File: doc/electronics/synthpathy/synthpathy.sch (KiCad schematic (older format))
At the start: 56 parts, among them J1 midi_in_port, J2 midi_out_port, SW1 btn0, SW10 btn9, SW11 btn10, SW12 btn11, SW13 btn12, SW14 btn13, SW15 btn14, SW16 btn15, SW17 btn16, SW18 btn17, SW19 btn18, SW2 btn1, SW20 btn19, SW21 btn20, SW22 btn21, SW23 btn22, SW24 btn23, SW25 btn24, SW3 btn2, SW4 btn3, SW5 btn4, SW6 btn5, SW7 btn6, SW8 btn7, SW9 btn8, U1 Raspberry Pico, U2 4N35

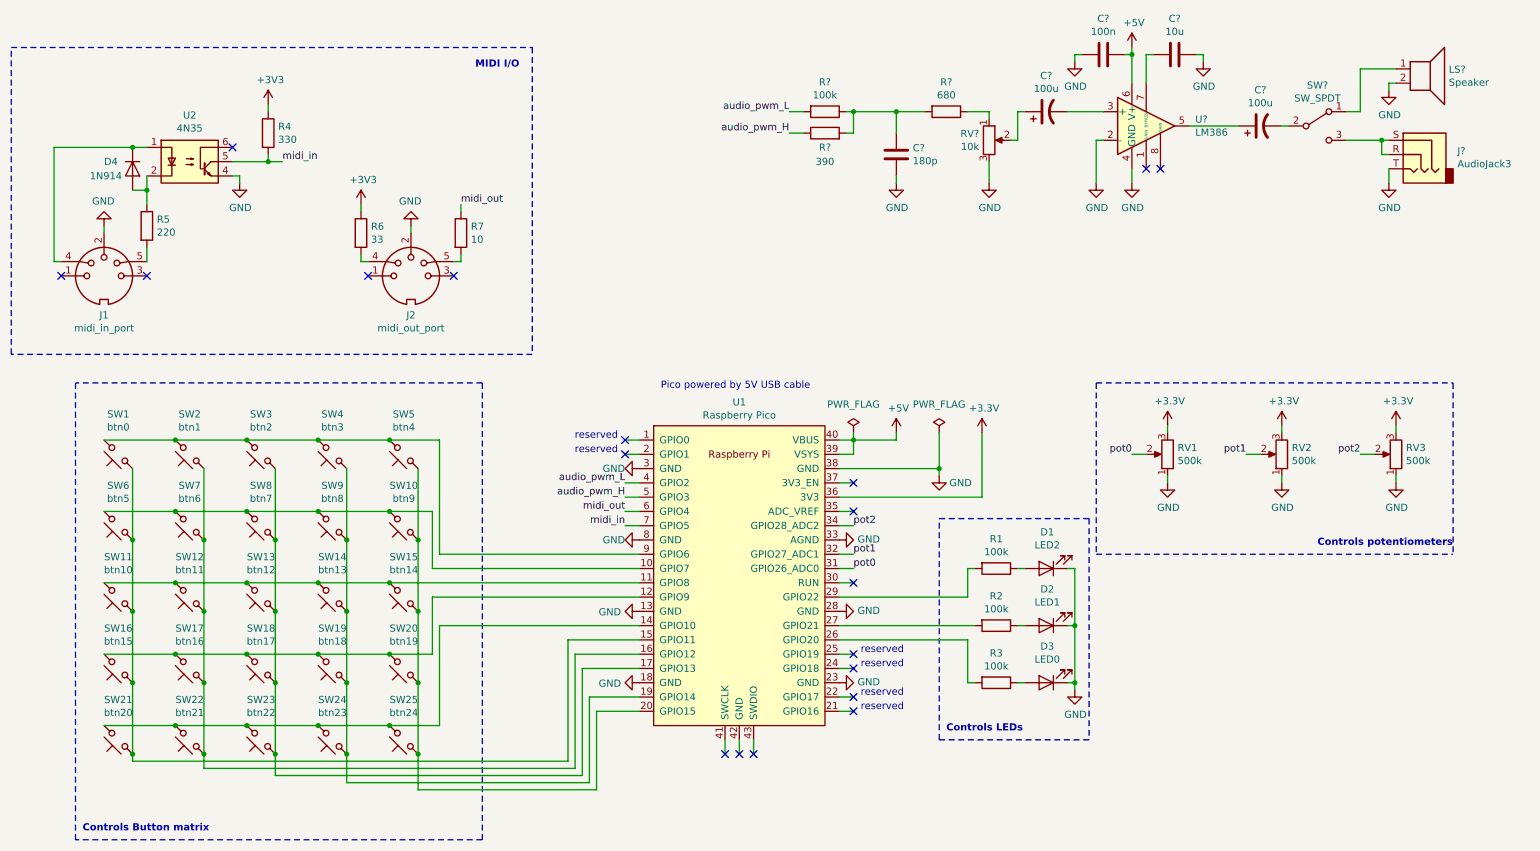
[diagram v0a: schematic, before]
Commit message: Updated schematics and comments
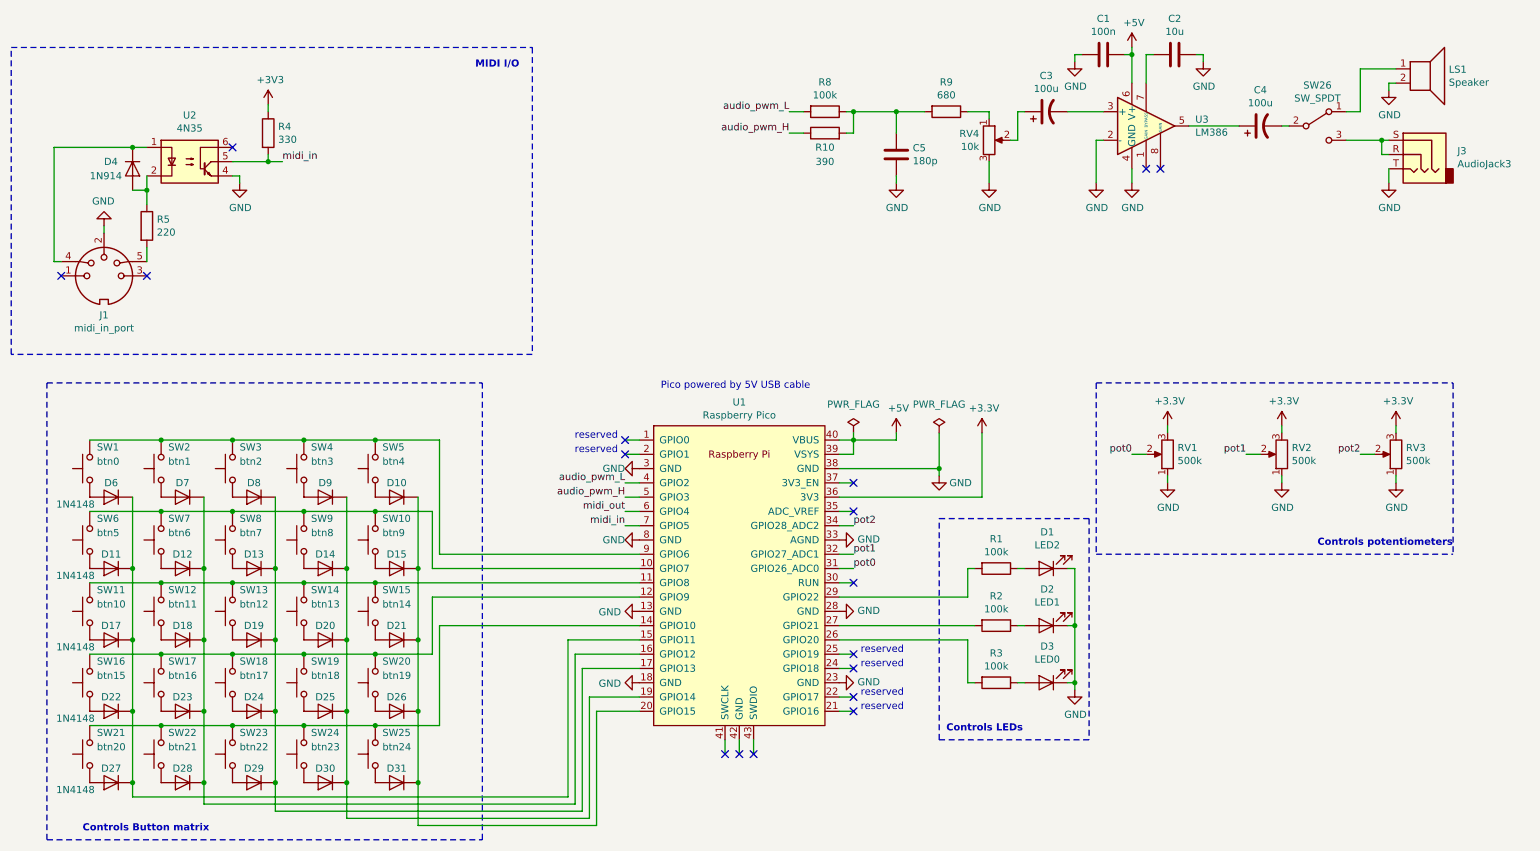
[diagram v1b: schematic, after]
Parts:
- removed J2: midi_out_port, symbol Connector:DIN-5_180degree
- removed R6: 33, symbol Device:R
- removed R7: 10, symbol Device:R
- removed SW1: btn0, symbol Switch:SW_Push_45deg
- removed SW10: btn9, symbol Switch:SW_Push_45deg
- removed SW11: btn10, symbol Switch:SW_Push_45deg
- removed SW12: btn11, symbol Switch:SW_Push_45deg
- removed SW13: btn12, symbol Switch:SW_Push_45deg
- removed SW14: btn13, symbol Switch:SW_Push_45deg
- removed SW15: btn14, symbol Switch:SW_Push_45deg
- removed SW16: btn15, symbol Switch:SW_Push_45deg
- removed SW17: btn16, symbol Switch:SW_Push_45deg
- removed SW18: btn17, symbol Switch:SW_Push_45deg
- removed SW19: btn18, symbol Switch:SW_Push_45deg
- removed SW2: btn1, symbol Switch:SW_Push_45deg
- removed SW20: btn19, symbol Switch:SW_Push_45deg
- removed SW21: btn20, symbol Switch:SW_Push_45deg
- removed SW22: btn21, symbol Switch:SW_Push_45deg
- removed SW23: btn22, symbol Switch:SW_Push_45deg
- removed SW24: btn23, symbol Switch:SW_Push_45deg
- removed SW25: btn24, symbol Switch:SW_Push_45deg
- removed SW3: btn2, symbol Switch:SW_Push_45deg
- removed SW4: btn3, symbol Switch:SW_Push_45deg
- removed SW5: btn4, symbol Switch:SW_Push_45deg
- removed SW6: btn5, symbol Switch:SW_Push_45deg
- removed SW7: btn6, symbol Switch:SW_Push_45deg
- removed SW8: btn7, symbol Switch:SW_Push_45deg
- removed SW9: btn8, symbol Switch:SW_Push_45deg
- added D10, D11, D12, D13, D14, D15, D17, D18, D19, D20, D21, D22, D23, D24, D25, D26, D27, D28, D29, D30, D31, D6, D7, D8, D9: 1N4148, Diode_THT:D_DO-35_SOD27_P7.62mm_Horizontal, symbol Diode:1N4148
- added SW1: btn0, symbol Switch:SW_Push
- added SW10: btn9, symbol Switch:SW_Push
- added SW11: btn10, symbol Switch:SW_Push
- added SW12: btn11, symbol Switch:SW_Push
- added SW13: btn12, symbol Switch:SW_Push
- added SW14: btn13, symbol Switch:SW_Push
- added SW15: btn14, symbol Switch:SW_Push
- added SW16: btn15, symbol Switch:SW_Push
- added SW17: btn16, symbol Switch:SW_Push
- added SW18: btn17, symbol Switch:SW_Push
- added SW19: btn18, symbol Switch:SW_Push
- added SW2: btn1, symbol Switch:SW_Push
- added SW20: btn19, symbol Switch:SW_Push
- added SW21: btn20, symbol Switch:SW_Push
- added SW22: btn21, symbol Switch:SW_Push
- added SW23: btn22, symbol Switch:SW_Push
- added SW24: btn23, symbol Switch:SW_Push
- added SW25: btn24, symbol Switch:SW_Push
- added SW3: btn2, symbol Switch:SW_Push
- added SW4: btn3, symbol Switch:SW_Push
- added SW5: btn4, symbol Switch:SW_Push
- added SW6: btn5, symbol Switch:SW_Push
- added SW7: btn6, symbol Switch:SW_Push
- added SW8: btn7, symbol Switch:SW_Push
- added SW9: btn8, symbol Switch:SW_Push
- gave numbers to parts that had none: 13
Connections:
- net at U1.10 (GPIO7): now also SW10.2, SW6.2, SW7.2, SW8.2, SW9.2
- net at U1.11 (GPIO8): now also SW11.2, SW12.2, SW13.2, SW14.2, SW15.2
- net at U1.12 (GPIO9): now also SW16.2, SW17.2, SW18.2, SW19.2, SW20.2
- net at U1.14 (GPIO10): now also SW21.2, SW22.2, SW23.2, SW24.2, SW25.2
- net at U1.15 (GPIO11): now also D11.1 (K), D17.1 (K), D22.1 (K), D27.1 (K), D6.1 (K)
- net at U1.16 (GPIO12): now also D12.1 (K), D18.1 (K), D23.1 (K), D28.1 (K), D7.1 (K)
- net at U1.17 (GPIO13): now also D13.1 (K), D19.1 (K), D24.1 (K), D29.1 (K), D8.1 (K)
- net at U1.19 (GPIO14): now also D14.1 (K), D20.1 (K), D25.1 (K), D30.1 (K), D9.1 (K)
- net at U1.20 (GPIO15): now also D10.1 (K), D15.1 (K), D21.1 (K), D26.1 (K), D31.1 (K)
- net at U1.9 (GPIO6): now also SW1.2, SW2.2, SW3.2, SW4.2, SW5.2
- new net: D10.2 (A), SW5.1
- new net: D9.2 (A), SW4.1
- new net: D8.2 (A), SW3.1
- new net: D7.2 (A), SW2.1
- new net: D6.2 (A), SW1.1
- new net: D11.2 (A), SW6.1
- new net: D12.2 (A), SW7.1
- new net: D13.2 (A), SW8.1
- new net: D14.2 (A), SW9.1
- new net: D15.2 (A), SW10.1
- new net: D21.2 (A), SW15.1
- new net: D20.2 (A), SW14.1
- new net: D19.2 (A), SW13.1
- new net: D18.2 (A), SW12.1
- new net: D17.2 (A), SW11.1
- new net: D26.2 (A), SW20.1
- new net: D25.2 (A), SW19.1
- new net: D24.2 (A), SW18.1
- new net: D23.2 (A), SW17.1
- new net: D22.2 (A), SW16.1
- new net: D31.2 (A), SW25.1
- new net: D30.2 (A), SW24.1
- new net: D29.2 (A), SW23.1
- new net: D28.2 (A), SW22.1
- new net: D27.2 (A), SW21.1
- no-connect marks 19 -> 17
